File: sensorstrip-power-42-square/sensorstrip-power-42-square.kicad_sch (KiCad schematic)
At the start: 13 parts, among them J1 USB_C_Receptacle_PowerOnly, J2 Conn_01x02_MountingPin, J3 Conn_01x02_MountingPin, J4 Conn_01x02_MountingPin, J5 Conn_01x02_MountingPin, SW1 SW_DP3T

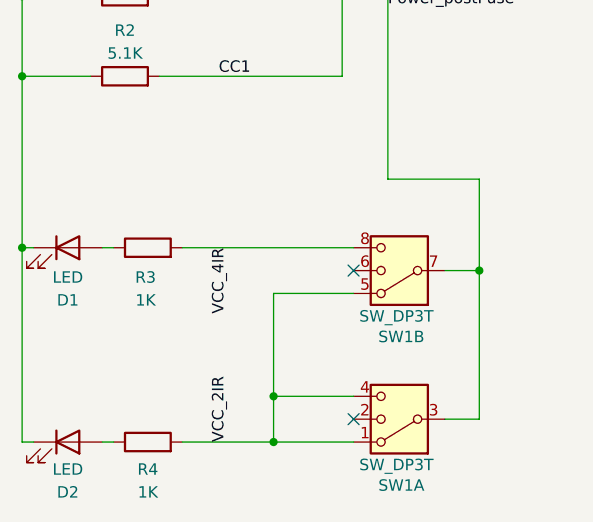
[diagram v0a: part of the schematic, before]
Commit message: Update 2/4IR square board for consistent status LED behaviour
Update DP3T switch footprint to make installing JS203011SCQN easier

Rename 2IR/4IR diamond layout board for clarity
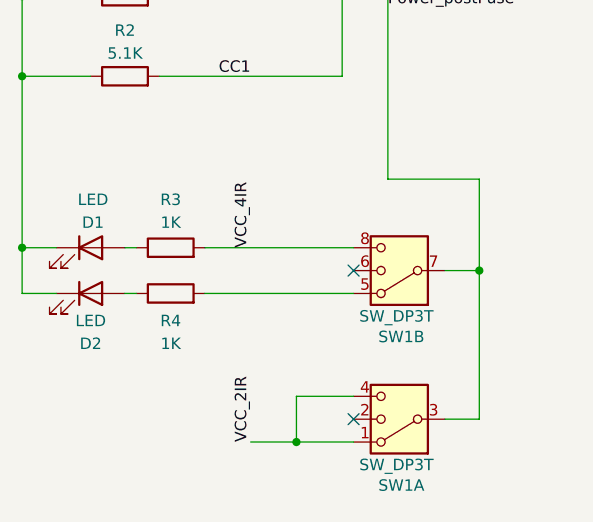
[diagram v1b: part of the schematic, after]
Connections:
- net VCC_2IR: no longer R4.2, SW1.5
- new net: R4.2, SW1.5
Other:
- moved on the sheet: D1, D2, R3, R4
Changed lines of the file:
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@@
 	(paper "A4")
-	(junction
-		(at 102.87 118.11)
-		(diameter 0)
-		(color 0 0 0 0)
-	)
 	(junction
 		(at 125.73 99.06)
@@
 	)
 	(junction
-		(at 102.87 113.03)
-		(diameter 0)
-		(color 0 0 0 0)
-	)
-	(junction
 		(at 88.9 59.69)
 		(diameter 0)
@@
 		(color 0 0 0 0)
 	)
+	(junction
+		(at 105.41 118.11)
+		(diameter 0)
+		(color 0 0 0 0)
+	)
 	(no_connect
 		(at 111.76 99.06)
@@
 	(wire
 		(pts
+			(xy 74.93 96.52) (xy 78.74 96.52)
+		)
+		(stroke
+			(width 0)
+			(type default)
+		)
+	)
+	(wire
+		(pts
 			(xy 101.6 59.69) (xy 101.6 57.15)
 		)
@@
 	(wire
 		(pts
-			(xy 74.93 96.52) (xy 76.2 96.52)
-		)
-		(stroke
-			(width 0)
-			(type default)
-		)
-	)
-	(wire
-		(pts
-			(xy 92.71 118.11) (xy 102.87 118.11)
+			(xy 86.36 101.6) (xy 87.63 101.6)
+		)
+		(stroke
+			(width 0)
+			(type default)
+		)
+	)
+	(wire
+		(pts
+			(xy 105.41 118.11) (xy 111.76 118.11)
+		)
+		(stroke
+			(width 0)
+			(type default)
+		)
+	)
+	(wire
+		(pts
+			(xy 105.41 113.03) (xy 105.41 118.11)
 		)
 		(stroke
@@
 	(wire
 		(pts
-			(xy 74.93 118.11) (xy 74.93 96.52)
-		)
-		(stroke
-			(width 0)
-			(type default)
-		)
-	)
-	(wire
-		(pts
 			(xy 180.34 86.36) (xy 175.26 86.36)
 		)
@@
 	(wire
 		(pts
-			(xy 102.87 101.6) (xy 102.87 113.03)
-		)
-		(stroke
-			(width 0)
-			(type default)
-		)
-	)
-	(wire
-		(pts
 			(xy 115.57 88.9) (xy 125.73 88.9)
 		)
@@
 	(wire
 		(pts
-			(xy 92.71 96.52) (xy 111.76 96.52)
-		)
-		(stroke
-			(width 0)
-			(type default)
-		)
-	)
-	(wire
-		(pts
 			(xy 74.93 77.47) (xy 82.55 77.47)
 		)
@@
 	(wire
 		(pts
+			(xy 86.36 96.52) (xy 87.63 96.52)
+		)
+		(stroke
+			(width 0)
+			(type default)
+		)
+	)
+	(wire
+		(pts
 			(xy 74.93 68.58) (xy 74.93 77.47)
 		)
@@
 	(wire
 		(pts
-			(xy 111.76 101.6) (xy 102.87 101.6)
+			(xy 100.33 118.11) (xy 105.41 118.11)
 		)
 		(stroke
@@
 	(wire
 		(pts
+			(xy 74.93 101.6) (xy 74.93 96.52)
+		)
+		(stroke
+			(width 0)
+			(type default)
+		)
+	)
+	(wire
+		(pts
 			(xy 121.92 99.06) (xy 125.73 99.06)
 		)
@@
 	(wire
 		(pts
-			(xy 83.82 118.11) (xy 85.09 118.11)
-		)
-		(stroke
-			(width 0)
-			(type default)
-		)
-	)
-	(wire
-		(pts
 			(xy 175.26 100.33) (xy 175.26 95.25)
 		)
@@
 	(wire
 		(pts
+			(xy 95.25 96.52) (xy 111.76 96.52)
+		)
+		(stroke
+			(width 0)
+			(type default)
+		)
+	)
+	(wire
+		(pts
 			(xy 110.49 77.47) (xy 90.17 77.47)
 		)
@@
 	(wire
 		(pts
-			(xy 102.87 113.03) (xy 111.76 113.03)
+			(xy 74.93 101.6) (xy 78.74 101.6)
 		)
 		(stroke
@@
 	(wire
 		(pts
-			(xy 74.93 118.11) (xy 76.2 118.11)
-		)
-		(stroke
-			(width 0)
-			(type default)
-		)
-	)
-	(wire
-		(pts
 			(xy 88.9 59.69) (xy 91.44 59.69)
 		)
@@
 	(wire
 		(pts
-			(xy 102.87 113.03) (xy 102.87 118.11)
-		)
-		(stroke
-			(width 0)
-			(type default)
-		)
-	)
-	(wire
-		(pts
-			(xy 83.82 96.52) (xy 85.09 96.52)
-		)
-		(stroke
-			(width 0)
-			(type default)
-		)
-	)
-	(wire
-		(pts
 			(xy 121.92 115.57) (xy 125.73 115.57)
 		)
@@
 	(wire
 		(pts
+			(xy 95.25 101.6) (xy 111.76 101.6)
+		)
+		(stroke
+			(width 0)
+			(type default)
+		)
+	)
+	(wire
+		(pts
+			(xy 111.76 113.03) (xy 105.41 113.03)
+		)
+		(stroke
+			(width 0)
+			(type default)
+		)
+	)
+	(wire
+		(pts
 			(xy 106.68 68.58) (xy 90.17 68.58)
 		)
@@
 		(pts
 			(xy 74.93 68.58) (xy 74.93 59.69)
-		)
-		(stroke
-			(width 0)
-			(type default)
-		)
-	)
-	(wire
-		(pts
-			(xy 111.76 118.11) (xy 102.87 118.11)
 		)
 		(stroke
@@
 	)
 	(label "VCC_4IR"
-		(at 97.79 96.52 270)
+		(at 100.33 96.52 90)
 		(fields_autoplaced yes)
 		(effects
@@
 				(size 1.27 1.27)
 			)
-			(justify right bottom)
+			(justify left bottom)
 		)
 	)
 	(label "VCC_2IR"
-		(at 97.79 118.11 90)
+		(at 100.33 118.11 90)
 		(fields_autoplaced yes)
 		(effects
@@
 	(symbol
 		(lib_id "Device:LED")
-		(at 80.01 96.52 0)
+		(at 82.55 96.52 0)
 		(unit 1)
 		(exclude_from_sim no)
@@
 		(dnp no)
 		(property "Reference" "D1"
-			(at 80.01 102.362 0)
+			(at 82.804 93.726 0)
 			(effects
 				(font
@@
 		)
 		(property "Value" "LED"
-			(at 80.01 99.822 0)
+			(at 82.804 91.186 0)
 			(effects
 				(font
@@
 		)
 		(property "Footprint" "LED_SMD:LED_0603_1608Metric_Pad1.05x0.95mm_HandSolder"
-			(at 80.01 96.52 0)
+			(at 82.55 96.52 0)
 			(effects
 				(font
@@
 		)
 		(property "Datasheet" "~"
-			(at 80.01 96.52 0)
+			(at 82.55 96.52 0)
 			(effects
 				(font
@@
 		)
 		(property "Description" "Light emitting diode"
-			(at 80.01 96.52 0)
+			(at 82.55 96.52 0)
 			(effects
 				(font
@@
 	(symbol
 		(lib_id "Device:R")
-		(at 88.9 118.11 90)
+		(at 91.44 101.6 90)
 		(unit 1)
 		(exclude_from_sim no)
@@
 		(dnp no)
 		(property "Reference" "R4"
-			(at 88.9 121.158 90)
+			(at 91.44 104.648 90)
 			(effects
 				(font
@@
 		)
 		(property "Value" "1K"
-			(at 88.9 123.698 90)
+			(at 91.44 107.188 90)
 			(effects
 				(font
@@
 		)
 		(property "Footprint" "Resistor_SMD:R_0603_1608Metric_Pad0.98x0.95mm_HandSolder"
-			(at 88.9 119.888 90)
+			(at 91.44 103.378 90)
 			(effects
 				(font
@@
 		)
 		(property "Datasheet" "~"
-			(at 88.9 118.11 0)
+			(at 91.44 101.6 0)
 			(effects
 				(font
@@
 		)
 		(property "Description" ""
-			(at 88.9 118.11 0)
+			(at 91.44 101.6 0)
 			(effects
 				(font
@@
 	(symbol
 		(lib_id "Device:R")
-		(at 88.9 96.52 90)
+		(at 91.44 96.52 90)
 		(unit 1)
 		(exclude_from_sim no)
@@
 		(dnp no)
 		(property "Reference" "R3"
-			(at 88.646 99.822 90)
+			(at 91.44 91.186 90)
 			(effects
 				(font
@@
 		)
 		(property "Value" "1K"
-			(at 88.646 102.362 90)
+			(at 91.44 93.726 90)
 			(effects
 				(font
@@
 		)
 		(property "Footprint" "Resistor_SMD:R_0603_1608Metric_Pad0.98x0.95mm_HandSolder"
-			(at 88.9 98.298 90)
+			(at 91.44 98.298 90)
 			(effects
 				(font
@@
 		)
 		(property "Datasheet" "~"
-			(at 88.9 96.52 0)
+			(at 91.44 96.52 0)
 			(effects
 				(font
@@
 		)
 		(property "Description" ""
-			(at 88.9 96.52 0)
+			(at 91.44 96.52 0)
 			(effects
 				(font
@@
 	(symbol
 		(lib_id "Device:LED")
-		(at 80.01 118.11 0)
+		(at 82.55 101.6 0)
 		(unit 1)
 		(exclude_from_sim no)
@@
 		(dnp no)
 		(property "Reference" "D2"
-			(at 80.01 123.698 0)
+			(at 82.55 107.188 0)
 			(effects
 				(font
@@
 		)
 		(property "Value" "LED"
-			(at 80.01 121.158 0)
+			(at 82.55 104.648 0)
 			(effects
 				(font
@@
 		)
 		(property "Footprint" "LED_SMD:LED_0603_1608Metric_Pad1.05x0.95mm_HandSolder"
-			(at 80.01 118.11 0)
+			(at 82.55 101.6 0)
 			(effects
 				(font
@@
 		)
 		(property "Datasheet" "~"
-			(at 80.01 118.11 0)
+			(at 82.55 101.6 0)
 			(effects
 				(font
@@
 		)
 		(property "Description" "Light emitting diode"
-			(at 80.01 118.11 0)
-			(effects
-				(font
+			(at 82.55 101.6 0)
+			(effects
+				(font
